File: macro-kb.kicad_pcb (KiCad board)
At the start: 2 copper layers, 68.3 x 49.2 mm, 53 parts, among them SW1 SW_Push, U1 ATmega32U2-MU, Y1 16MHz 18pF

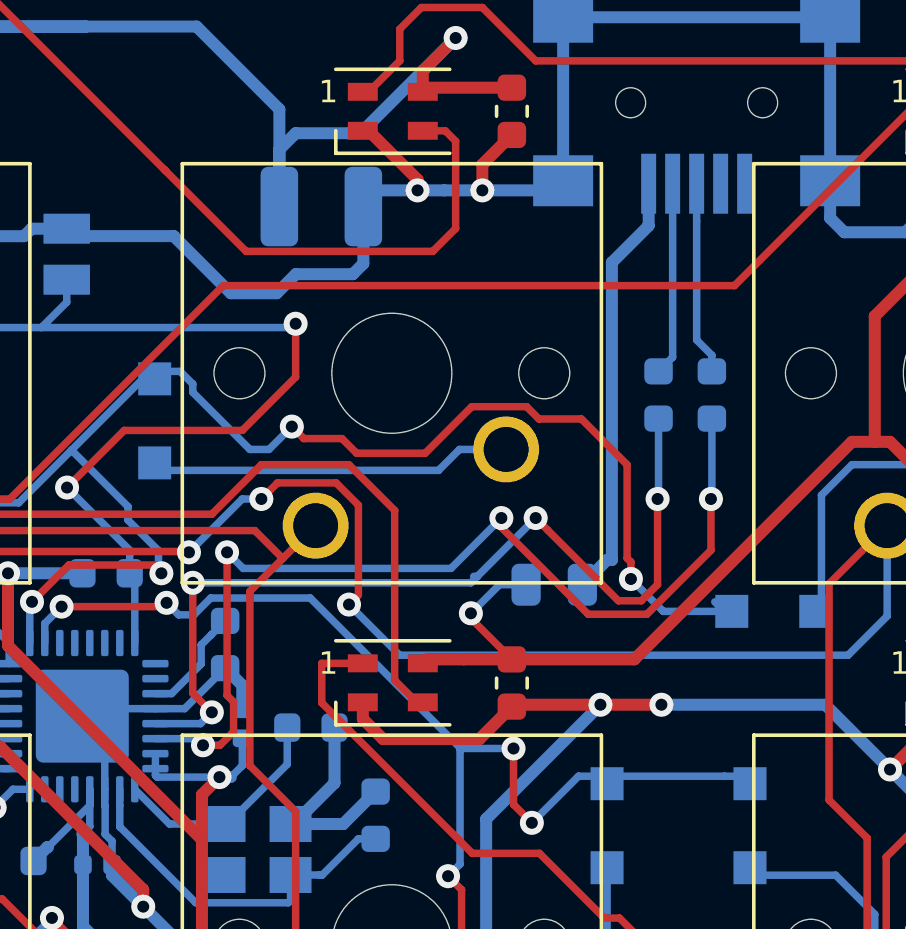
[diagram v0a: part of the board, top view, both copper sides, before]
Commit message: fixed crossed USB lines v1.1
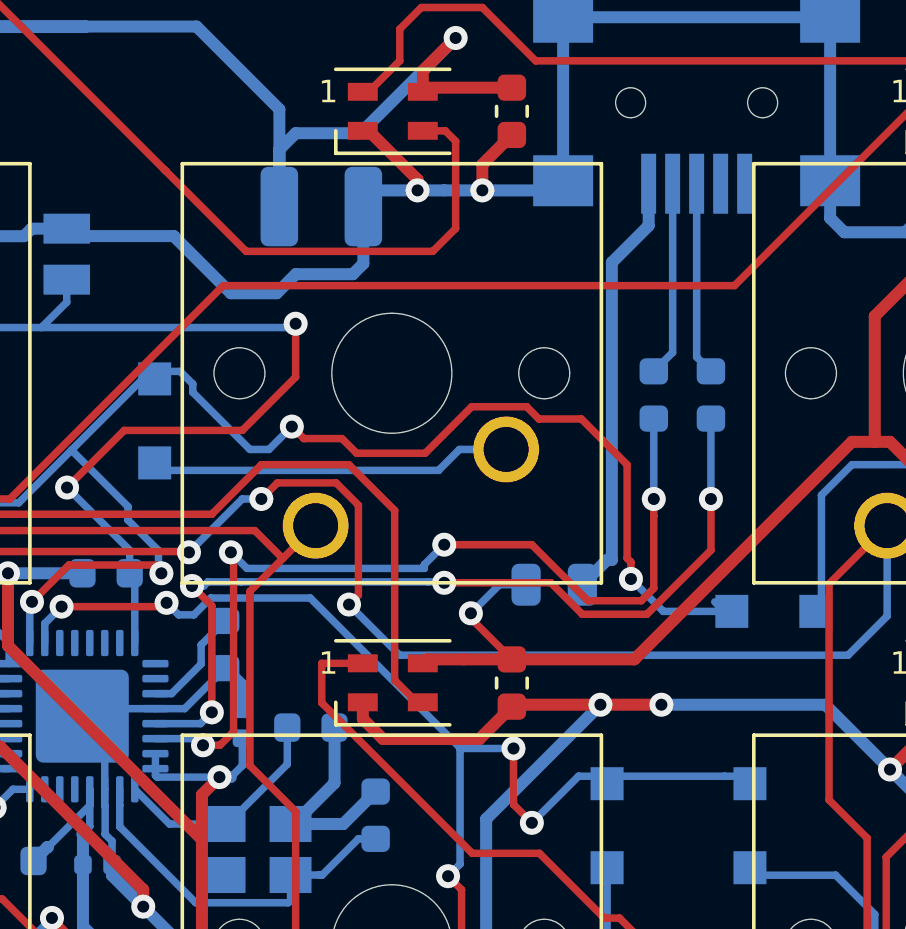
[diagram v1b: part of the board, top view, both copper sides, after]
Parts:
- moved R3 1.94 mm to (142.7, 90.9)
- moved R2 1.75 mm to (144.6, 90.9)
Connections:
- USB1 pad 2: D+ -> D-
- USB1 pad 3: D- -> D+
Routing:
- net Net-(R3-Pad1): track 32.8 -> 30.2 mm
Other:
- board text added: "macroKB version 1.1"
- board text removed: "macroKB version 1.0"
